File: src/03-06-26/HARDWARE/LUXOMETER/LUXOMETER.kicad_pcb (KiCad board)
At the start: 2 copper layers, 70 x 65 mm, 11 parts, among them U2 RS485_TRANSCEIVER

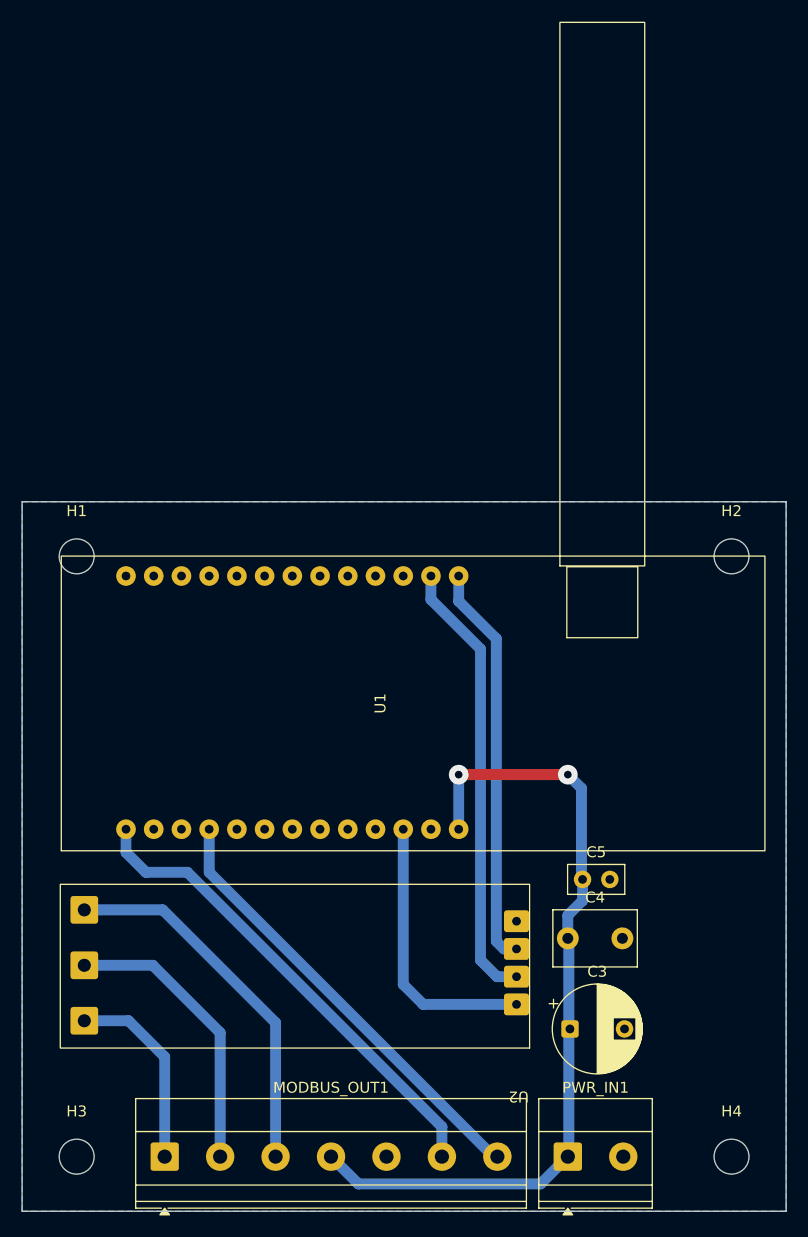
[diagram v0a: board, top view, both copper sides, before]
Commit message: Changes to the PCB
- DEV_MODULE_EXAPLE_SLAVE added
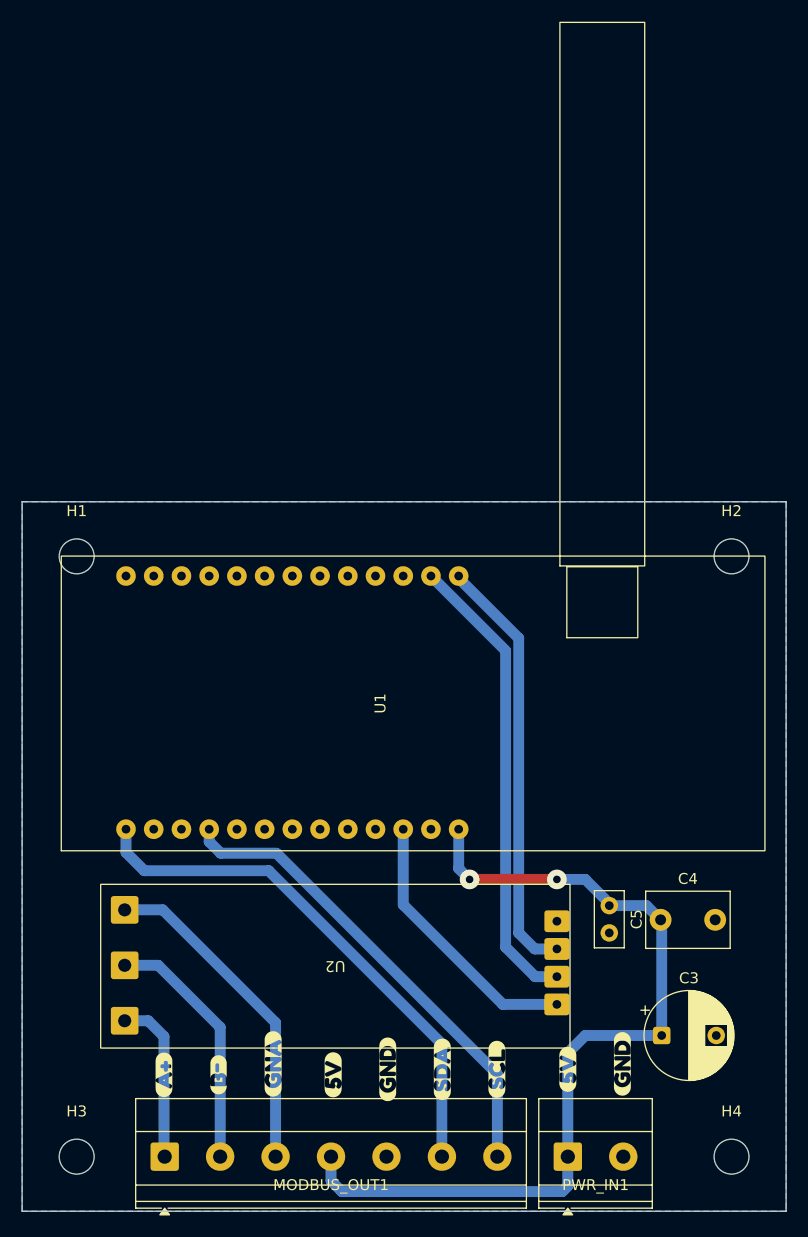
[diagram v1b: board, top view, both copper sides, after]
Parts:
- added kibuzzard-6A2423AA: G***, kibuzzard-6A2423AA, F.Cu at (103.0, 92.5)
- added kibuzzard-6A2423C2: G***, kibuzzard-6A2423C2, F.Cu at (98.0, 92.5)
- added kibuzzard-6A2424E2: G***, kibuzzard-6A2424E2, F.Cu at (108.0, 91.5)
- added kibuzzard-6A2424EE: G***, kibuzzard-6A2424EE, F.Cu at (135.0, 92.0)
- added kibuzzard-6A2424EE: G***, kibuzzard-6A2424EE, F.Cu at (113.5, 92.5)
- added kibuzzard-6A2424FA: G***, kibuzzard-6A2424FA, F.Cu at (140.0, 91.5)
- added kibuzzard-6A2424FA: G***, kibuzzard-6A2424FA, F.Cu at (118.5, 92.0)
- added kibuzzard-6A24251B: G***, kibuzzard-6A24251B, F.Cu at (123.5, 92.0)
- added kibuzzard-6A24252A: G***, kibuzzard-6A24252A, F.Cu at (128.5, 92.0)
- moved C4 8.67 mm to (143.5, 78.3)
- moved C3 8.42 mm to (143.6, 88.9)
- moved U2 3.70 mm to (113.7, 90.0)
- moved C5 3.43 mm to (138.8, 77.0), turned to -90 degrees
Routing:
- net +5V: track 75.0 -> 80.8 mm
- net SDA: track 44.2 -> 48.7 mm
- net GND_T: track 34.1 -> 30.4 mm
- net B-: track 26.4 -> 23.0 mm
- net SCL: track 41.1 -> 43.9 mm
- net A+: track 17.9 -> 15.2 mm
- net RX: track 37.0 -> 39.1 mm
- net TX: track 41.0 -> 42.7 mm
- net +3.3V: track 25.4 -> 24.8 mm
